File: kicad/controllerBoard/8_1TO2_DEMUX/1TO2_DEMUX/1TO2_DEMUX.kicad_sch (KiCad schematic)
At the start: 10 parts, among them Q1 PMOS, Q10 NMOS, Q2 PMOS, Q3 NMOS, Q4 NMOS, Q5 PMOS, Q6 PMOS, Q7 NMOS, Q8 NMOS, Q9 PMOS

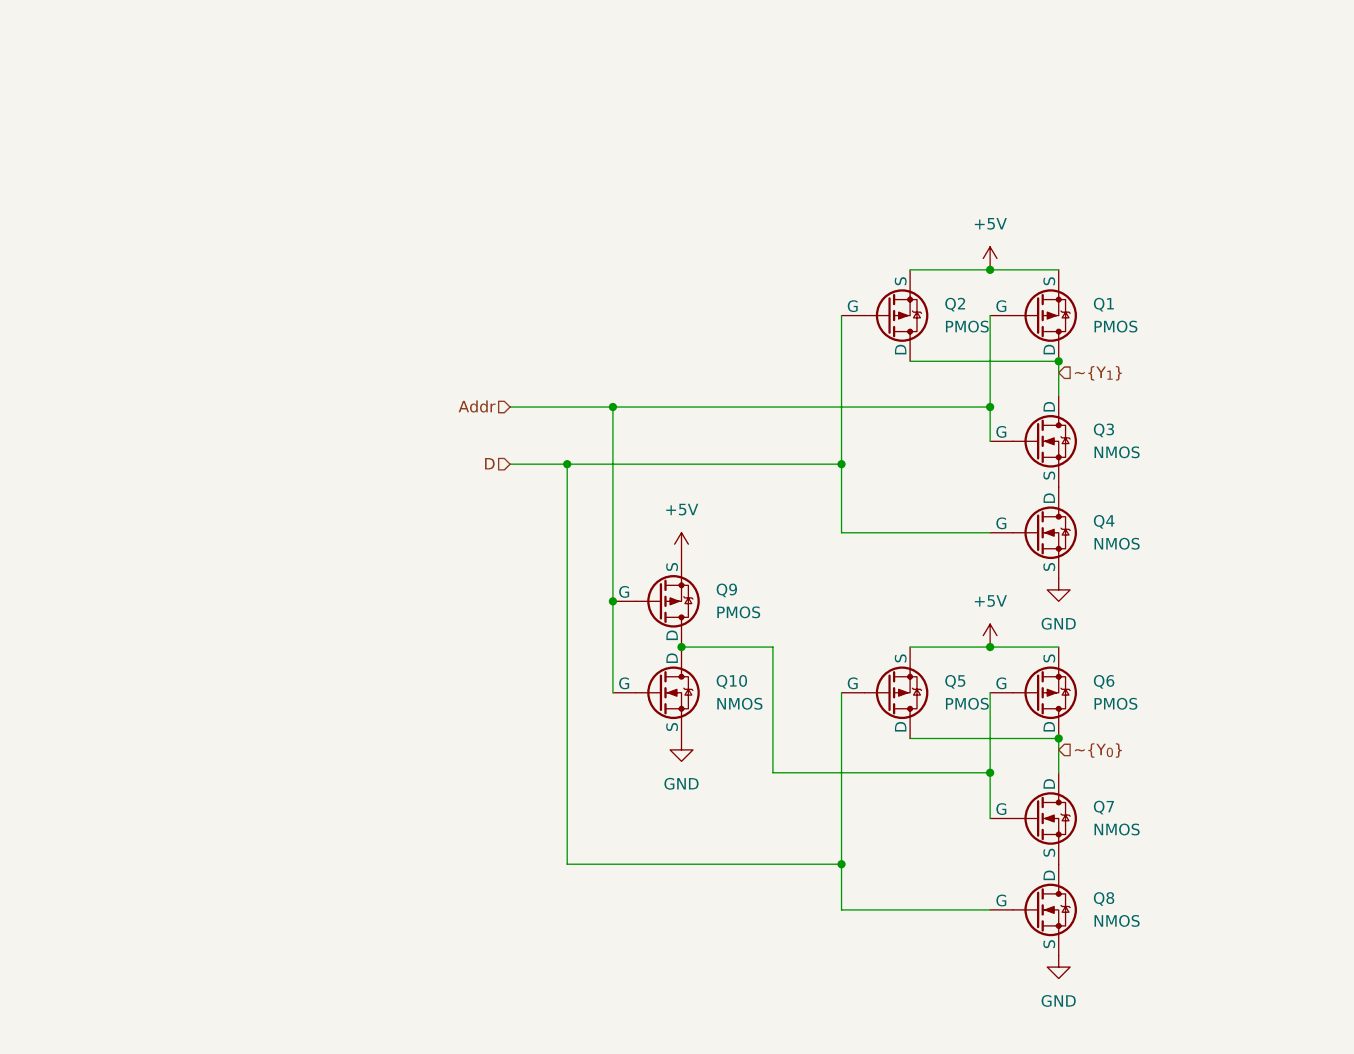
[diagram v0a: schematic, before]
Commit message: finish address to bit line decoder
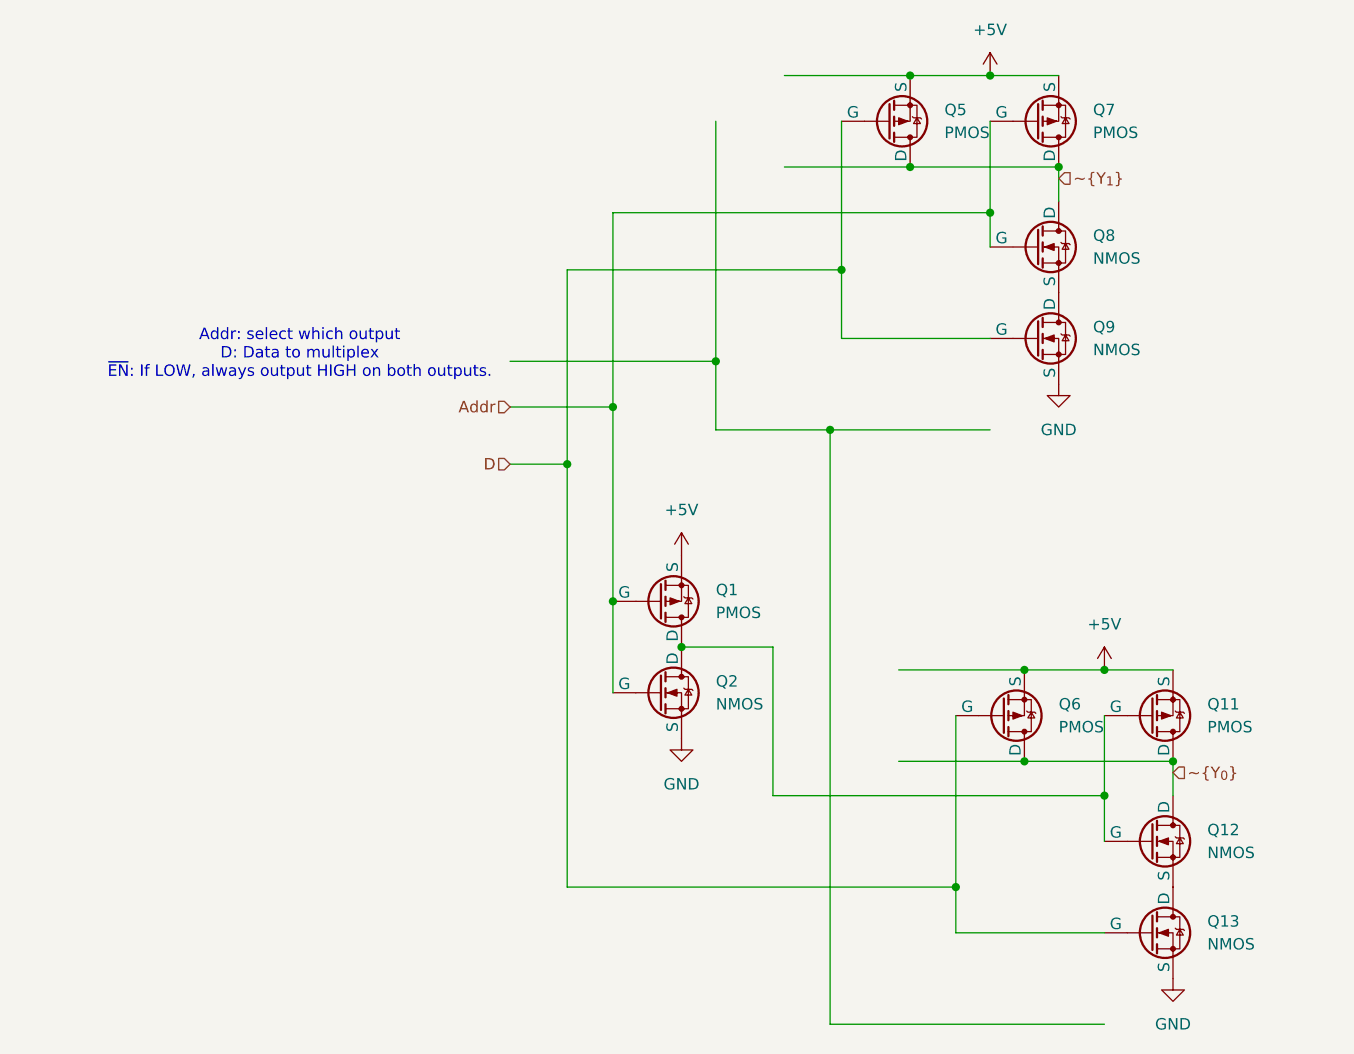
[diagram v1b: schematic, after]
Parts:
- renumbered Q9 to Q1, Q6 to Q11, Q7 to Q12, Q8 to Q13, Q10 to Q2, Q2 to Q5, Q5 to Q6, Q1 to Q7, Q3 to Q8, Q4 to Q9
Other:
- note added: "Addr: select which output D: Data to multiplex ~{EN}: If LOW, always output HIGH on both outputs."
- moved on the sheet: Q11, Q12, Q13, Q5, Q6, Q7, Q8, Q9

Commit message: demux
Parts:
- renumbered Q1 to Q15, Q2 to Q16, Q5 to Q19, Q6 to Q20, Q7 to Q21, Q8 to Q22, Q9 to Q23, Q11 to Q25, Q12 to Q26, Q13 to Q27
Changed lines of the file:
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@@
 		(dnp no)
 		(fields_autoplaced yes)
-		(property "Reference" "Q12"
+		(property "Reference" "Q26"
 			(at 140.97 110.4899 0)
 			(show_name no)
@@
 		(dnp no)
 		(fields_autoplaced yes)
-		(property "Reference" "Q6"
+		(property "Reference" "Q20"
 			(at 124.46 96.5199 0)
 			(show_name no)
@@
 		(dnp no)
 		(fields_autoplaced yes)
-		(property "Reference" "Q7"
+		(property "Reference" "Q21"
 			(at 128.27 30.4799 0)
 			(show_name no)
@@
 		(dnp no)
 		(fields_autoplaced yes)
-		(property "Reference" "#PWR04"
+		(property "Reference" "#PWR010"
 			(at 82.55 83.82 0)
 			(hide yes)
@@
 		(dnp no)
 		(fields_autoplaced yes)
-		(property "Reference" "#PWR09"
+		(property "Reference" "#PWR015"
 			(at 137.16 133.35 0)
 			(hide yes)
@@
 		(dnp no)
 		(fields_autoplaced yes)
-		(property "Reference" "#PWR07"
+		(property "Reference" "#PWR013"
 			(at 124.46 67.31 0)
 			(hide yes)
@@
 		(dnp no)
 		(fields_autoplaced yes)
-		(property "Reference" "Q8"
+		(property "Reference" "Q22"
 			(at 128.27 44.4499 0)
 			(show_name no)
@@
 		(dnp no)
 		(fields_autoplaced yes)
-		(property "Reference" "Q11"
+		(property "Reference" "Q25"
 			(at 140.97 96.5199 0)
 			(show_name no)
@@
 		(dnp no)
 		(fields_autoplaced yes)
-		(property "Reference" "Q9"
+		(property "Reference" "Q23"
 			(at 128.27 54.6099 0)
 			(show_name no)
@@
 		(dnp no)
 		(fields_autoplaced yes)
-		(property "Reference" "Q5"
+		(property "Reference" "Q19"
 			(at 111.76 30.4799 0)
 			(show_name no)
@@
 		(dnp no)
 		(fields_autoplaced yes)
-		(property "Reference" "#PWR08"
+		(property "Reference" "#PWR014"
 			(at 129.54 96.52 0)
 			(hide yes)
@@
 		(dnp no)
 		(fields_autoplaced yes)
-		(property "Reference" "Q2"
+		(property "Reference" "Q16"
 			(at 86.36 93.9799 0)
 			(show_name no)
@@
 		(dnp no)
 		(fields_autoplaced yes)
-		(property "Reference" "Q13"
+		(property "Reference" "Q27"
 			(at 140.97 120.6499 0)
 			(show_name no)
@@
 		(dnp no)
 		(fields_autoplaced yes)
-		(property "Reference" "#PWR06"
+		(property "Reference" "#PWR012"
 			(at 116.84 30.48 0)
 			(hide yes)
@@
 		(dnp no)
 		(fields_autoplaced yes)
-		(property "Reference" "Q1"
+		(property "Reference" "Q15"
 			(at 86.36 83.8199 0)
 			(show_name no)
@@
 		(dnp no)
 		(fields_autoplaced yes)
-		(property "Reference" "#PWR05"
+		(property "Reference" "#PWR011"
 			(at 82.55 106.68 0)
 			(hide yes)

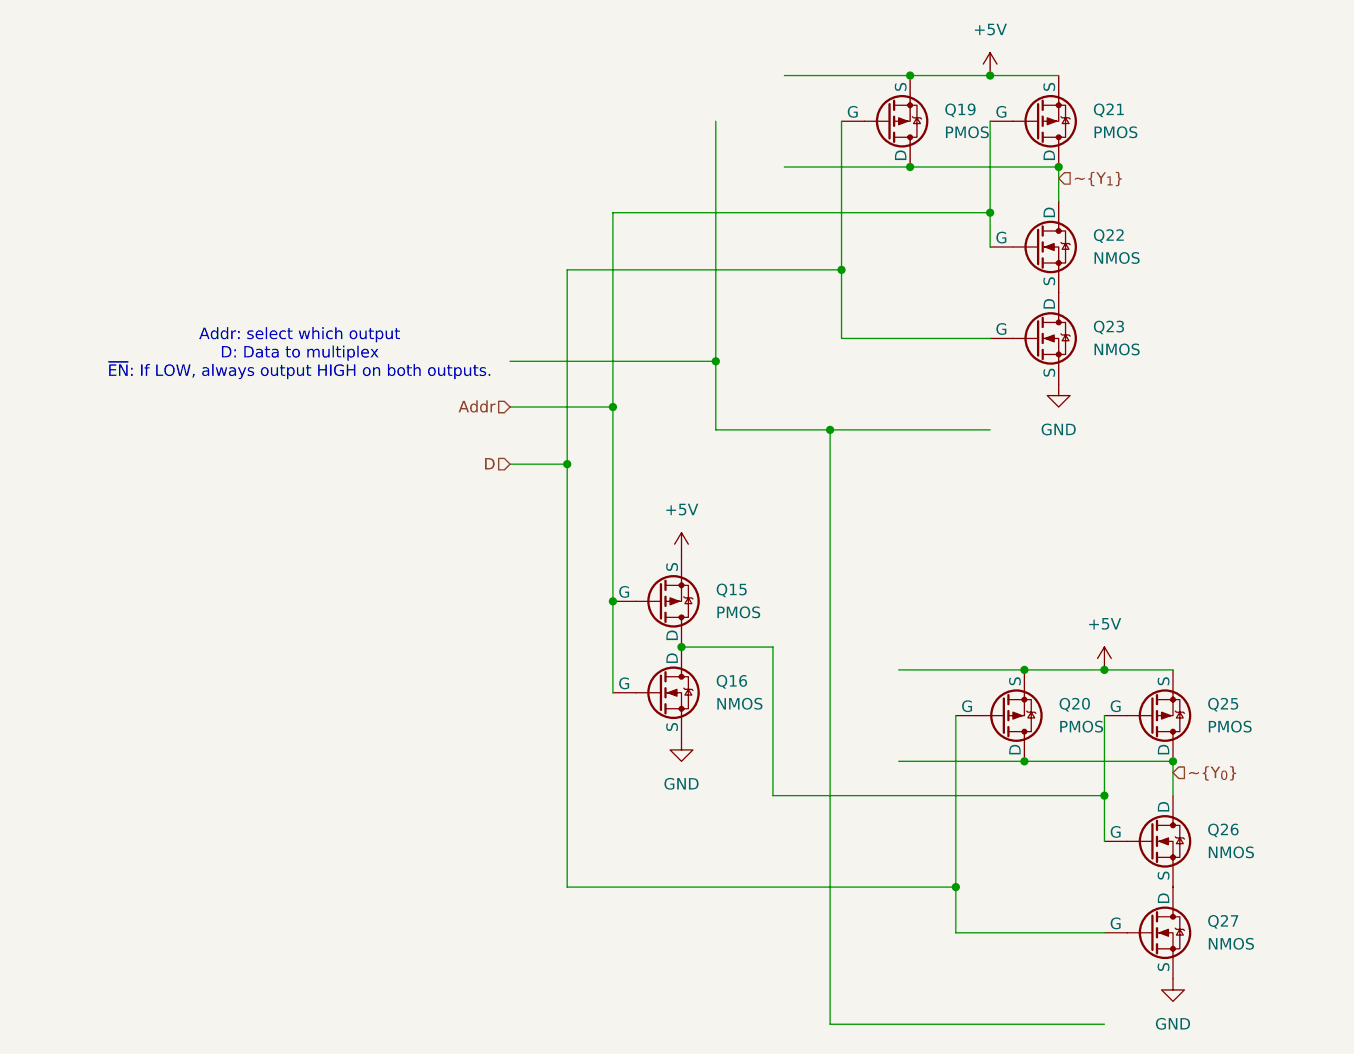
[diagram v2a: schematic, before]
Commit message: Finish input stage schematic
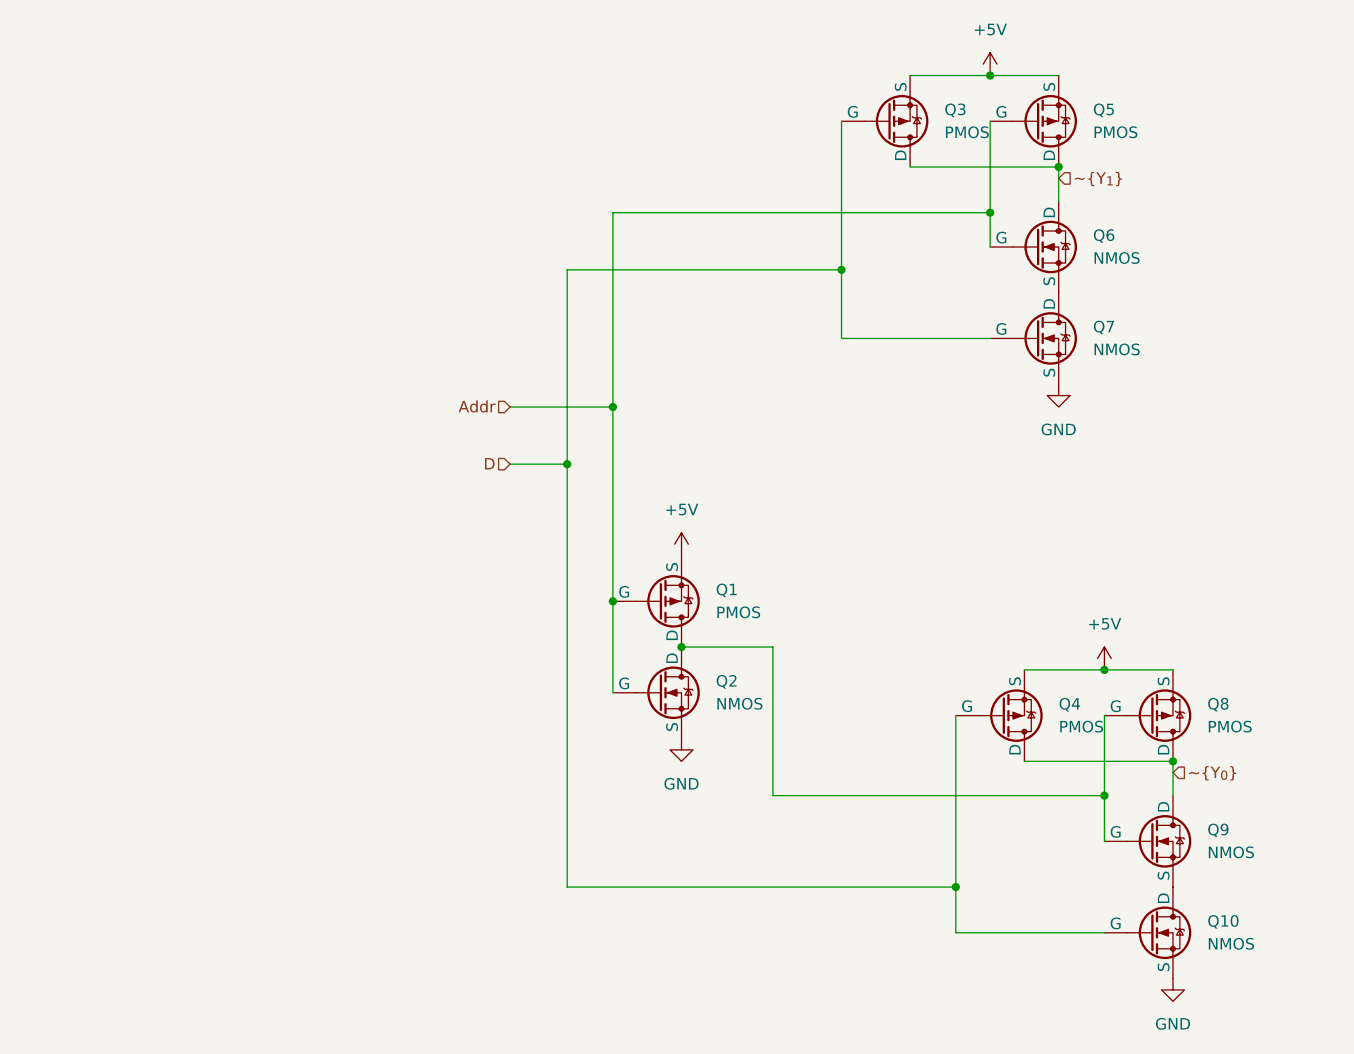
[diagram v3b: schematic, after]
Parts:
- renumbered Q15 to Q1, Q27 to Q10, Q16 to Q2, Q19 to Q3, Q20 to Q4, Q21 to Q5, Q22 to Q6, Q23 to Q7, Q25 to Q8, Q26 to Q9
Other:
- note removed: "Addr: select which output D: Data to multiplex ~{EN}: If LOW, always output HIGH on both outputs."

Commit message: did stuff
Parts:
- renumbered Q9 to Q10, Q10 to Q11, Q1 to Q2, Q2 to Q3, Q3 to Q4, Q4 to Q5, Q5 to Q6, Q6 to Q7, Q7 to Q8, Q8 to Q9

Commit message: did more simulation, added bom
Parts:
- renumbered Q2 to Q1, Q11 to Q10, Q3 to Q2, Q4 to Q3, Q5 to Q4, Q6 to Q5, Q7 to Q6, Q8 to Q7, Q9 to Q8, Q10 to Q9
